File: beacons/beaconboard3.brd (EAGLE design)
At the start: 101.6 x 76.2 mm, 31 parts, among them IC1 7805TV, Q1 2N3904, Q2 16MHz

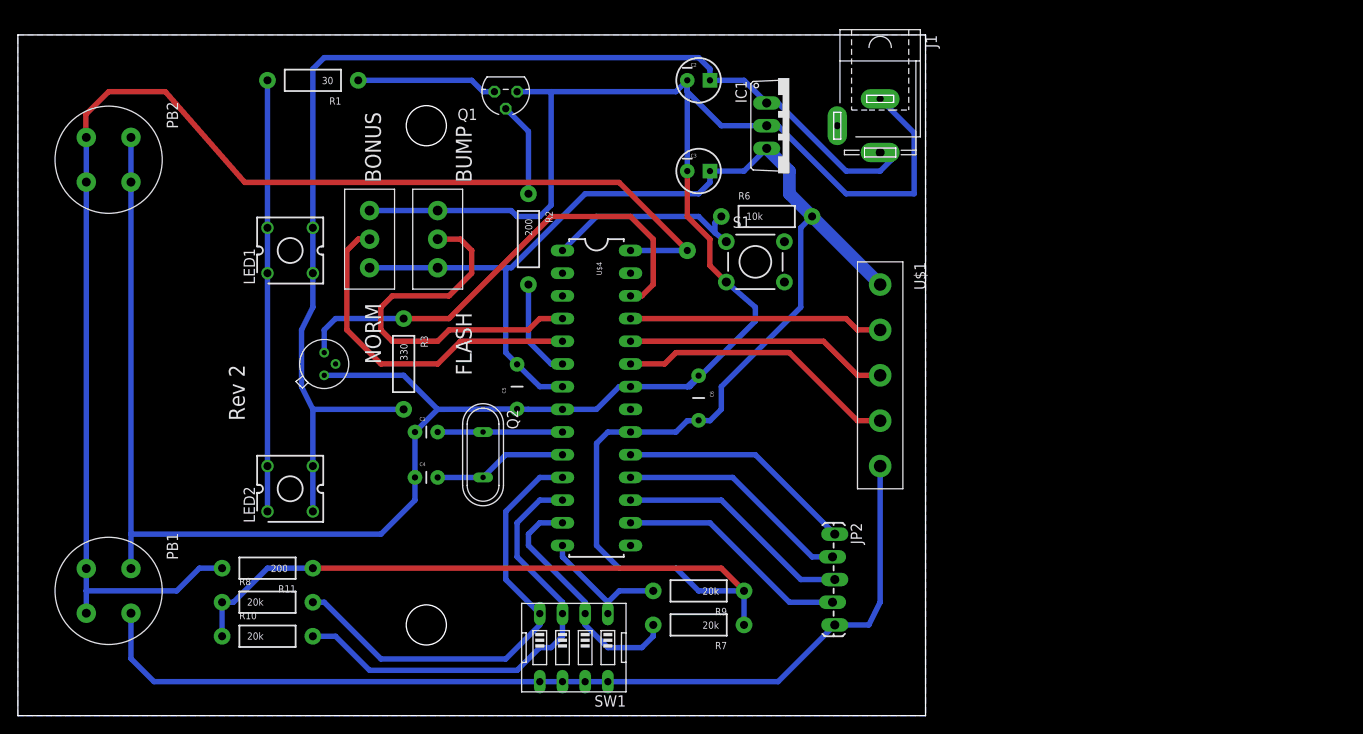
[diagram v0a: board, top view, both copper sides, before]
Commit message: Added beaconboard 3, extended version
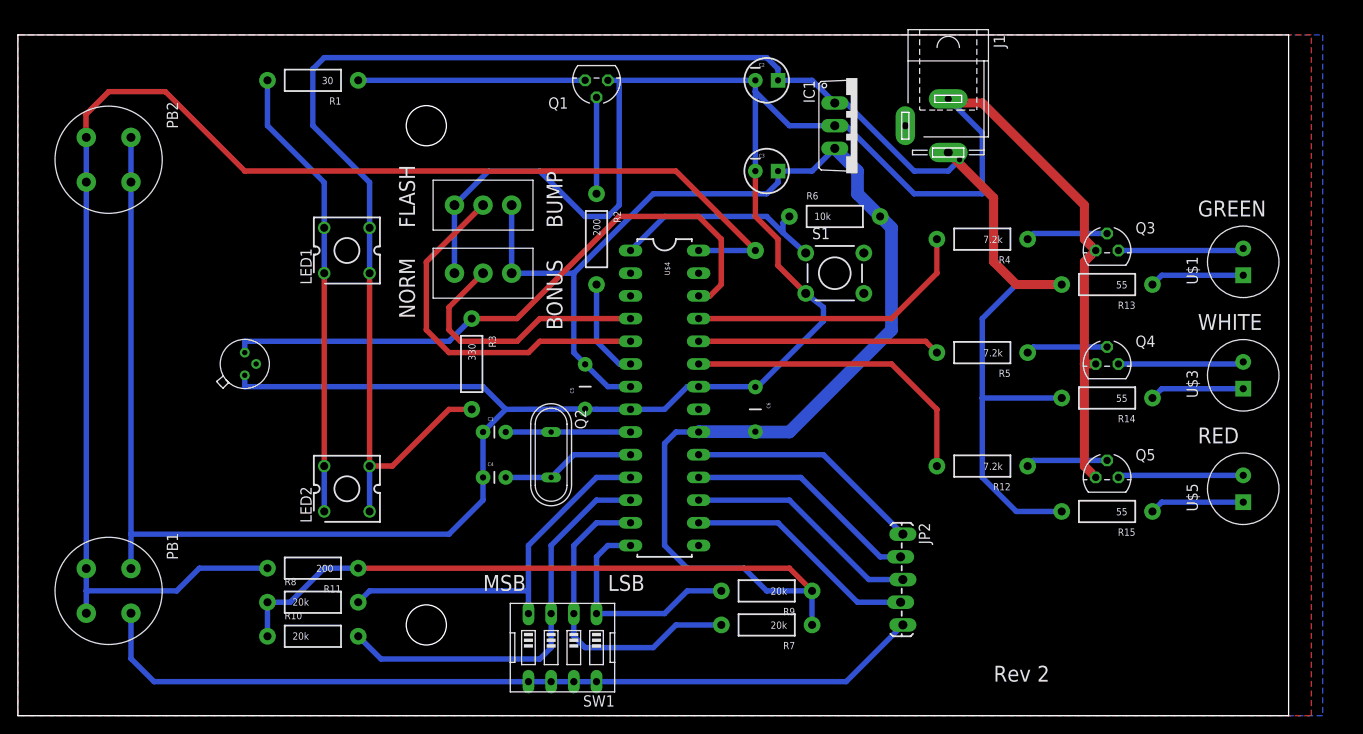
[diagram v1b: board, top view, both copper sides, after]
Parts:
- added Q3, Q4, Q5: 2N3904, transistor-small-signal:TO92D
- added R12, R4, R5: 7.2k, SparkFun-Resistors:AXIAL-0.4
- added R13, R14, R15: 55, SparkFun-Resistors:AXIAL-0.4
- added U$3, U$5: 8MM_LED, e11:8MM_LED
- U$1: value 1X5_3.5MM_TERMINAL_BLOCK -> 8MM_LED; device e11:1X5_3.5MM_TERMINAL_BLOCK -> e11:8MM_LED
- moved U$1 42.6 mm to (137.2, 50.8), turned to 90 degrees
- moved MODE2 13.3 mm to (52.1, 57.1), turned to 180 degrees
- moved Q1 10.2 mm to (64.8, 71.1)
- moved S1 8.98 mm to (91.4, 49.5)
- moved U$2 8.89 mm to (25.4, 39.4)
- moved IC1 7.62 mm to (94.0, 66.0)
- moved J1 7.62 mm to (104.1, 66.0)
- moved JP2 7.62 mm to (99.1, 20.3)
- moved R6 7.62 mm to (91.4, 55.9)
- moved U$4 7.62 mm to (72.4, 35.6)
- moved C1 7.62 mm to (52.1, 31.8)
- moved C4 7.62 mm to (52.1, 26.7)
- moved C5 7.62 mm to (63.5, 36.8)
- moved Q2 7.62 mm to (59.7, 29.2)
- moved R2 7.62 mm to (64.8, 53.3)
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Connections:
- new net LED_GRN: R4.P$2, U$4.25
- new net LED_RED: R12.P$2, U$4.23
- new net LED_WHT: R5.P$2, U$4.24
- new net N$10: Q5.B, R12.P$1
- new net N$21: Q5.C, U$5.NEG
- new net N$22: R13.P$1, U$1.POS
- new net N$23: R14.P$1, U$3.POS
- new net N$24: R15.P$1, U$5.POS
- new net N$8: Q4.B, R5.P$1
- net GND: now also Q3.E, Q4.E, Q5.E; no longer U$1.5
- net N$17: now also Q3.C, U$1.NEG; no longer U$1.4, U$4.23
- net N$18: now also Q4.C, U$3.NEG; no longer U$1.2, U$4.25
- net N$4: now also Q3.B, R4.P$1; no longer U$1.3, U$4.24
- net VCC: no longer U$1.1
- net VDD: now also R13.P$2, R14.P$2, R15.P$2
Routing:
- net VDD: track 133.6 -> 217.8 mm, vias 0 -> 1
- net GND: track 385.2 -> 453.7 mm
- net LED_RED: track 0.00 -> 35.1 mm
- net LED_GRN: track 0.00 -> 32.6 mm
- net LED_WHT: track 0.00 -> 27.2 mm
- net N$4: track 29.5 -> 9.15 mm
- net N$17: track 31.6 -> 14.1 mm
- net N$9: track 53.8 -> 69.6 mm
- net N$18: track 28.5 -> 14.1 mm
- net N$21: track 0.00 -> 14.1 mm
- net MODE1: track 43.1 -> 29.8 mm
- net BUMPER: track 154.6 -> 166.9 mm
- net N$24: track 0.00 -> 10.6 mm
- net N$23: track 0.00 -> 10.6 mm
- net N$22: track 0.00 -> 10.6 mm
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- added copper zone on layer 1, net GND
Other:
- board size 101.6 x 76.2 mm -> 142.2 x 76.2 mm
- board text added: "GREEN"
- board text added: "LSB"
- board text added: "MSB"
- board text added: "RED"
- board text added: "WHITE"

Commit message: Updated beaconboard with staff suggestions
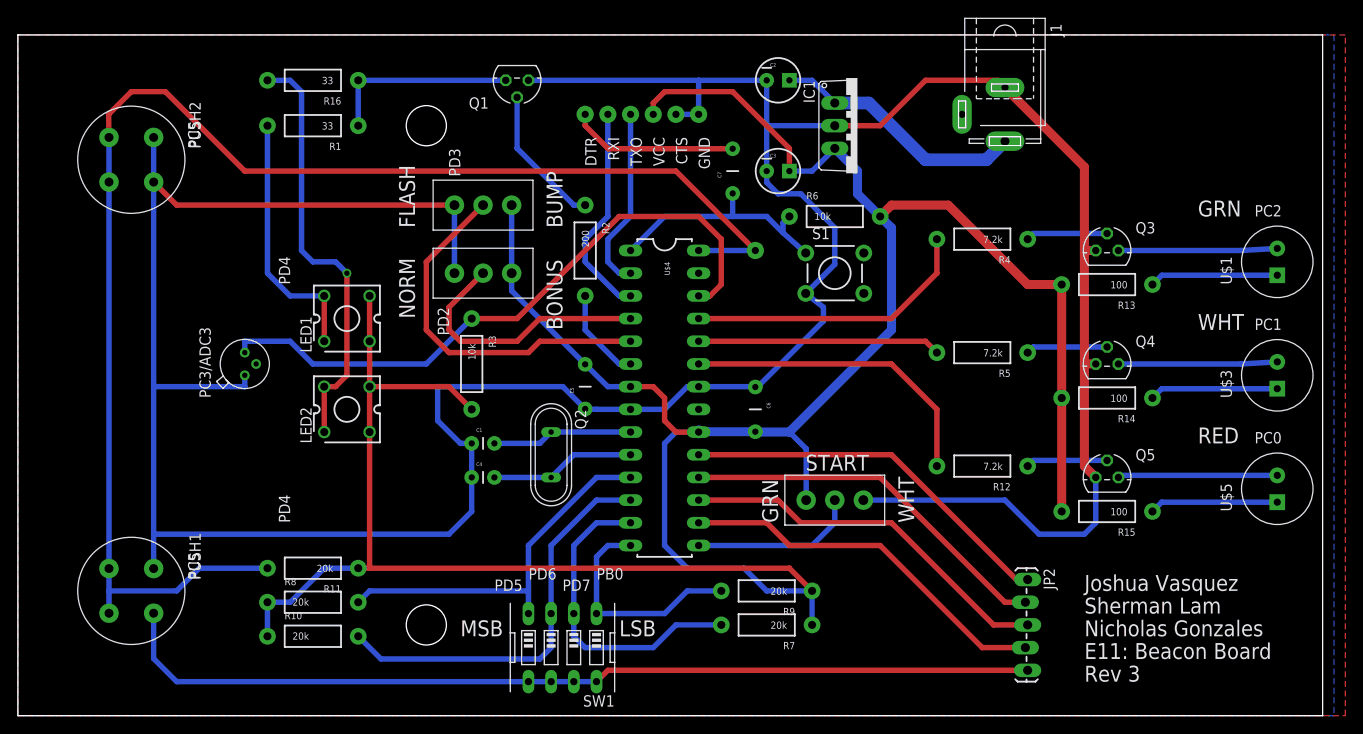
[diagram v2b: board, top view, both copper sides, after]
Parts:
- removed PB1, PB2: D6_PUSHBUTTON, e11:D6_PUSH_BUTTON
- added C7: 0.1uF, SparkFun-Passives:CAP-PTH-5MM
- added MODE3: SPD_SLIDE_SWITCH, e11:SPDT_SLIDE_SWITCH
- added PUSH1, PUSH2: D6_PUSHBUTTON, e11:D6_PUSH_BUTTON
- added R16: 33, SparkFun-Resistors:AXIAL-0.4
- added U$6: FTDI, e11:FTDI
- R1: value 30 -> 33
- R11: value 200 -> 20k
- R13, R14, R15: value 55 -> 100
- R3: value 330 -> 10k
- moved JP2 14.9 mm to (113.0, 15.2)
- moved LED2 8.89 mm to (36.8, 34.3)
- moved Q1 8.89 mm to (55.9, 71.1)
- moved LED1 7.62 mm to (36.8, 44.5)
- moved J1 6.48 mm to (110.5, 67.3)
- moved R1 5.08 mm to (33.0, 66.0)
- moved U$1 3.81 mm to (141.0, 50.8)
- moved U$3 3.81 mm to (141.0, 38.1)
- moved U$5 3.81 mm to (141.0, 25.4)
- moved C1 1.80 mm to (50.8, 30.5)
- moved R2 1.80 mm to (63.5, 52.1)
- moved C2 1.27 mm to (85.1, 71.1)
- moved C3 1.27 mm to (85.1, 61.0)
- moved C4 1.27 mm to (50.8, 26.7)
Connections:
- new net DTR: C7.2, U$6.DTR
- new net MODE3: MODE3.2, U$4.15
- new net N$25: LED2.1, LED2.4, R16.P$2
- new net RXI: U$4.2, U$6.TXO
- new net TXO: U$4.3, U$6.RXI
- net BUMPER: now also PUSH1.3, PUSH1.4, PUSH2.3, PUSH2.4; no longer PB1.3, PB1.4, PB2.3, PB2.4
- net GND: now also MODE3.3, PUSH1.1, PUSH1.2, PUSH2.1, PUSH2.2, U$6.CTS, U$6.GND; no longer PB1.1, PB1.2, PB2.1, PB2.2
- net N$1: now also R16.P$1
- net N$11: now also C7.1
- net N$3: no longer LED2.1, LED2.4
- net VCC: now also LED1.2, LED1.3, LED2.2, LED2.3, MODE3.1, R13.P$2, R14.P$2, R15.P$2, R3.P$2, U$6.VCC
- net VDD: no longer LED1.2, LED1.3, LED2.2, LED2.3, R13.P$2, R14.P$2, R15.P$2, R3.P$2
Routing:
- net VDD: track 217.8 -> 28.7 mm, vias 1 -> 0
- net VCC: track 222.0 -> 323.1 mm
- net N$25: track 0.00 -> 47.8 mm, vias 0 -> 1
- net GND: track 453.7 -> 487.5 mm
- net TXO: track 0.00 -> 24.2 mm
- net N$3: track 50.9 -> 29.0 mm
- net RXI: track 0.00 -> 20.6 mm
- net DTR: track 0.00 -> 18.8 mm
- net MODE3: track 0.00 -> 18.8 mm
- net N$7: track 26.5 -> 42.6 mm
- net N$6: track 26.3 -> 42.4 mm
- net N$5: track 26.5 -> 42.6 mm
- net N$20: track 26.3 -> 42.4 mm
- net N$2: track 10.8 -> 16.0 mm
- net BUMPER: track 166.9 -> 161.8 mm
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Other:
- board size 142.2 x 76.2 mm -> 146.1 x 76.2 mm
- board text added: "GRN"
- board text added: "PB0"
- board text added: "PC0"
- board text added: "PC1"
- board text added: "PC2"
- board text added: "PC3/ADC3"
- board text added: "PC5"
- board text added: "PD2"
- board text added: "PD3"
- board text added: "PD4"
- board text added: "PD5"
- board text added: "PD6"
- board text added: "PD7"
- board text added: "Rev 3"
- board text added: "START"
- board text added: "WHT"
- board text removed: "GREEN"
- board text removed: "Rev 2"
- board text removed: "WHITE"
